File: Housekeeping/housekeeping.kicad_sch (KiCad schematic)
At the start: 2 parts

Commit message: DCDCconverter modified
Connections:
- net 9V renamed 12V
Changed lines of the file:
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@@
 		)
 	)
-	(hierarchical_label "9V"
+	(hierarchical_label "12V"
 		(shape input)
 		(at 133.35 80.01 180)
@@
 			(project "Supercap"
 				(path "/98ee8313-37ab-4329-91ab-b5710476f82f/47f13d7b-df0e-4361-81b8-c133778882c5"
-					(reference "P7809B-1000R")
-					(unit 1)
-				)
+					(reference "P7812B-1000R")
+					(unit 1)
+				)

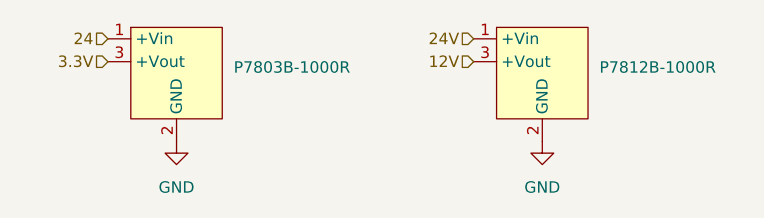
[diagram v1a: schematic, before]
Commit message: removed v1 files and assigned mouser part numbers
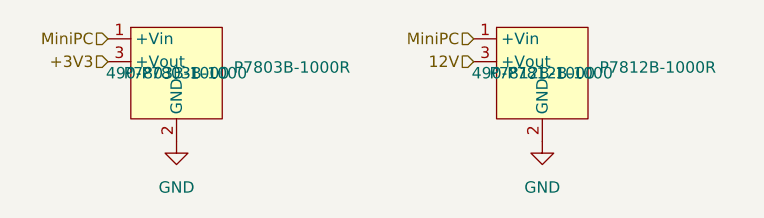
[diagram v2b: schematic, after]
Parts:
- P7803B-1000R: Manufacturer_Part_Number (none) -> P7803B-1000; Mouser Part Number (none) -> 490-P7803B-1000
- P7812B-1000R: Manufacturer_Part_Number (none) -> P7812B-1000; Mouser Part Number (none) -> 490-P7812B-1000
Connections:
- net 24V is gone; now on net MiniPC: P7812B-1000R.1 (+Vin)
- net 24 renamed MiniPC
- net 3.3V renamed +3V3
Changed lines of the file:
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@@
 	(generator_version "9.0")
 	(paper "A4")
-	(hierarchical_label "24"
+	(hierarchical_label "MiniPC"
 		(shape input)
 		(at 92.71 77.47 180)
@@
 		)
 	)
-	(hierarchical_label "3.3V"
+	(hierarchical_label "+3V3"
 		(shape input)
 		(at 92.71 80.01 180)
@@
 		)
 	)
-	(hierarchical_label "24V"
+	(hierarchical_label "MiniPC"
 		(shape input)
 		(at 133.35 77.47 180)
@@
 			)
 		)
+		(property "Manufacturer_Part_Number" "P7812B-1000"
+			(at 140.97 81.28 0)
+			(effects
+				(font
+					(size 1.27 1.27)
+				)
+			)
+		)
+		(property "Mouser Part Number" "490-P7812B-1000"
+			(at 140.97 81.28 0)
+			(effects
+				(font
+					(size 1.27 1.27)
+				)
+			)
+		)
 		(pin "1"
 		)
@@
 			)
 		)
+		(property "Manufacturer_Part_Number" "P7803B-1000"
+			(at 100.33 81.28 0)
+			(effects
+				(font
+					(size 1.27 1.27)
+				)
+			)
+		)
+		(property "Mouser Part Number" "490-P7803B-1000"
+			(at 100.33 81.28 0)
+			(effects
+				(font
+					(size 1.27 1.27)
+				)
+			)
+		)

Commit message: began layout
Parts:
- P7803B-1000R1: renamed from P7803B-1000R; value ~ -> P7803B-1000; footprint P78B-1000R series:P78B-1000R -> Robomaster_ICs:P7812B1000; symbol P78B-1000R series:P78B-1000R -> Robomaster_IV:P7803B-1000; Height (none) -> 10.45; Manufacturer_Name (none) -> CUI Inc.; Mouser Price/Stock (none) -> https://www.mouser.com/ProductDetail/CUI-Inc/P7803B-1000?qs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
- P7812B-1000R1: renamed from P7812B-1000R; value ~ -> 490-P7812B-1000; footprint P78B-1000R series:P78B-1000R -> Robomaster_ICs:P7812B1000; symbol P78B-1000R series:P78B-1000R -> Robomaster_IV:P7812B-1000; Height (none) -> 10.45; Manufacturer_Name (none) -> CUI Inc.; Mouser Price/Stock (none) -> https://www.mouser.com/ProductDetail/CUI-Inc/P7812B-1000?qs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
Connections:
- net 12V renamed +12V
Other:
- note added: "3V3 DC/DC"
- note added: "Gate Driver V_{cc} DC/DC"
- moved on the sheet: P7803B-1000R1, P7812B-1000R1

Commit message: mostly done with first order layout
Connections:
- net MiniPC: no longer P7812B-1000R1.1 (+VIN)
- new net +24V: P7812B-1000R1.1 (+VIN)
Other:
- company: (none) -> UT Robomaster
- title: (none) -> Housekeeping Board
- moved on the sheet: P7803B-1000R1, P7812B-1000R1
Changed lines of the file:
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@@
 	(generator_version "9.0")
 	(paper "A4")
+	(title_block
+		(title "Housekeeping Board")
+		(date "10/18/2025")
+		(rev "1")
+		(company "UT Robomaster")
+		(comment 1 "Robomaster")
+	)
 	(rectangle
-		(start 80.01 78.74)
-		(end 138.43 99.06)
+		(start 118.11 93.98)
+		(end 176.53 114.3)
 		(stroke
 			(width 0.635)
@@
 	)
 	(rectangle
-		(start 80.01 54.61)
-		(end 138.43 74.93)
+		(start 118.11 69.85)
+		(end 176.53 90.17)
 		(stroke
 			(width 0.635)
@@
 	(text "Gate Driver V_{cc} DC/DC"
 		(exclude_from_sim no)
-		(at 136.906 96.52 0)
+		(at 175.006 111.76 0)
 		(effects
 			(font
@@
 	(text "3V3 DC/DC"
 		(exclude_from_sim no)
-		(at 137.16 72.644 0)
+		(at 175.26 87.884 0)
 		(effects
 			(font
@@
 	(wire
 		(pts
-			(xy 92.71 91.44) (xy 92.71 86.36)
-		)
-		(stroke
-			(width 0)
-			(type default)
-		)
-	)
-	(wire
-		(pts
-			(xy 91.44 64.77) (xy 97.79 64.77)
-		)
-		(stroke
-			(width 0)
-			(type default)
-		)
-	)
-	(wire
-		(pts
-			(xy 93.98 62.23) (xy 93.98 67.31)
-		)
-		(stroke
-			(width 0)
-			(type default)
-		)
-	)
-	(wire
-		(pts
-			(xy 97.79 62.23) (xy 93.98 62.23)
-		)
-		(stroke
-			(width 0)
-			(type default)
-		)
-	)
-	(wire
-		(pts
-			(xy 90.17 88.9) (xy 96.52 88.9)
-		)
-		(stroke
-			(width 0)
-			(type default)
-		)
-	)
-	(wire
-		(pts
-			(xy 91.44 59.69) (xy 97.79 59.69)
-		)
-		(stroke
-			(width 0)
-			(type default)
-		)
-	)
-	(wire
-		(pts
-			(xy 92.71 86.36) (xy 96.52 86.36)
-		)
-		(stroke
-			(width 0)
-			(type default)
-		)
-	)
-	(wire
-		(pts
-			(xy 90.17 83.82) (xy 96.52 83.82)
+			(xy 130.81 106.68) (xy 130.81 101.6)
+		)
+		(stroke
+			(width 0)
+			(type default)
+		)
+	)
+	(wire
+		(pts
+			(xy 129.54 80.01) (xy 135.89 80.01)
+		)
+		(stroke
+			(width 0)
+			(type default)
+		)
+	)
+	(wire
+		(pts
+			(xy 132.08 77.47) (xy 132.08 82.55)
+		)
+		(stroke
+			(width 0)
+			(type default)
+		)
+	)
+	(wire
+		(pts
+			(xy 135.89 77.47) (xy 132.08 77.47)
+		)
+		(stroke
+			(width 0)
+			(type default)
+		)
+	)
+	(wire
+		(pts
+			(xy 128.27 104.14) (xy 134.62 104.14)
+		)
+		(stroke
+			(width 0)
+			(type default)
+		)
+	)
+	(wire
+		(pts
+			(xy 129.54 74.93) (xy 135.89 74.93)
+		)
+		(stroke
+			(width 0)
+			(type default)
+		)
+	)
+	(wire
+		(pts
+			(xy 130.81 101.6) (xy 134.62 101.6)
+		)
+		(stroke
+			(width 0)
+			(type default)
+		)
+	)
+	(wire
+		(pts
+			(xy 128.27 99.06) (xy 134.62 99.06)
 		)
 		(stroke
@@
 	(hierarchical_label "MiniPC"
 		(shape input)
-		(at 91.44 59.69 180)
+		(at 129.54 74.93 180)
 		(effects
 			(font
@@
 	(hierarchical_label "+3V3"
 		(shape input)
-		(at 91.44 64.77 180)
+		(at 129.54 80.01 180)
 		(effects
 			(font
@@
 		)
 	)
-	(hierarchical_label "MiniPC"
+	(hierarchical_label "+24V"
 		(shape input)
-		(at 90.17 83.82 180)
+		(at 128.27 99.06 180)
 		(effects
 			(font
@@
 	(hierarchical_label "+12V"
 		(shape input)
-		(at 90.17 88.9 180)
+		(at 128.27 104.14 180)
 		(effects
 			(font
@@
 	(symbol
 		(lib_id "power:GND")
-		(at 92.71 91.44 0)
+		(at 130.81 106.68 0)
 		(unit 1)
 		(exclude_from_sim no)
@@
 		(dnp no)
 		(fields_autoplaced yes)
-		(property "Reference" "#PWR015"
-			(at 92.71 97.79 0)
+		(property "Reference" "#PWR019"
+			(at 130.81 113.03 0)
 			(effects
 				(font
@@
 		)
 		(property "Value" "GND"
-			(at 92.71 96.52 0)
+			(at 130.81 111.76 0)
 			(effects
 				(font
@@
 		)
 		(property "Footprint" ""
-			(at 92.71 91.44 0)
+			(at 130.81 106.68 0)
 			(effects
 				(font
@@
 		)
 		(property "Datasheet" ""
-			(at 92.71 91.44 0)
+			(at 130.81 106.68 0)
 			(effects
 				(font
@@
 		)
 		(property "Description" "Power symbol creates a global label with name \"GND\" , ground"
-			(at 92.71 91.44 0)
+			(at 130.81 106.68 0)
 			(effects
 				(font
@@
 			(project ""
 				(path "/98ee8313-37ab-4329-91ab-b5710476f82f/47f13d7b-df0e-4361-81b8-c133778882c5"
-					(reference "#PWR015")
+					(reference "#PWR019")
 					(unit 1)
 				)
@@
 	(symbol
 		(lib_id "power:GND")
-		(at 93.98 67.31 0)
+		(at 132.08 82.55 0)
 		(unit 1)
 		(exclude_from_sim no)
@@
 		(dnp no)
 		(fields_autoplaced yes)
-		(property "Reference" "#PWR016"
-			(at 93.98 73.66 0)
+		(property "Reference" "#PWR020"
+			(at 132.08 88.9 0)
 			(effects
 				(font
@@
 		)
 		(property "Value" "GND"
-			(at 93.98 72.39 0)
+			(at 132.08 87.63 0)
 			(effects
 				(font
@@
 		)
 		(property "Footprint" ""
-			(at 93.98 67.31 0)
+			(at 132.08 82.55 0)
 			(effects
 				(font
@@
 		)
 		(property "Datasheet" ""
-			(at 93.98 67.31 0)
+			(at 132.08 82.55 0)
 			(effects
 				(font
@@
 		)
 		(property "Description" "Power symbol creates a global label with name \"GND\" , ground"
-			(at 93.98 67.31 0)
+			(at 132.08 82.55 0)
 			(effects
 				(font
@@
 			(project "Supercap"
 				(path "/98ee8313-37ab-4329-91ab-b5710476f82f/47f13d7b-df0e-4361-81b8-c133778882c5"
-					(reference "#PWR016")
+					(reference "#PWR020")
 					(unit 1)
 				)
@@
 		(lib_name "P7812B-1000_1")
 		(lib_id "Robomaster_IV:P7812B-1000")
-		(at 96.52 83.82 0)
+		(at 134.62 99.06 0)
 		(unit 1)
 		(exclude_from_sim no)
@@
 		(fields_autoplaced yes)
 		(property "Reference" "P7812B-1000R1"
-			(at 118.11 85.0899 0)
+			(at 156.21 100.3299 0)
 			(effects
 				(font
@@
 		)
 		(property "Value" "490-P7812B-1000"
-			(at 118.11 87.6299 0)
+			(at 156.21 102.8699 0)
 			(effects
 				(font
@@
 		)
 		(property "Footprint" "Robomaster_ICs:P7812B1000"
-			(at 118.11 178.74 0)
+			(at 156.21 193.98 0)
 			(effects
 				(font
@@
 		)
 		(property "Datasheet" "https://www.cui.com/product/resource/p78b-1000.pdf"
-			(at 118.11 278.74 0)
+			(at 156.21 293.98 0)
 			(effects
 				(font
@@
 		)
 		(property "Description" "Non-Isolated DC/DC Converters dc-dc non-isolated, 1.0 A, 15-32 Vdc input, 12 Vdc output, SIP"
-			(at 96.52 83.82 0)
+			(at 134.62 99.06 0)
 			(effects
 				(font
@@
 		)
 		(property "Manufacturer_Part_Number" "P7812B-1000"
-			(at 118.11 878.74 0)
+			(at 156.21 893.98 0)
 			(effects
 				(font
@@
 		)
 		(property "Mouser Part Number" "490-P7812B-1000"
-			(at 118.11 578.74 0)
+			(at 156.21 593.98 0)
 			(effects
 				(font
@@
 		)
 		(property "Height" "10.45"
-			(at 118.11 478.74 0)
+			(at 156.21 493.98 0)
 			(effects
 				(font
@@
 		)
 		(property "Mouser Price/Stock" "https://www.mouser.com/ProductDetail/CUI-Inc/P7812B-1000?qs=IKkN%2F947nfBpDKODYyx3RQ%3D%3D"
-			(at 118.11 678.74 0)
+			(at 156.21 693.98 0)
 			(effects
 				(font
@@
 		)
 		(property "Manufacturer_Name" "CUI Inc."
-			(at 118.11 778.74 0)
+			(at 156.21 793.98 0)
 			(effects
 				(font
@@
 	(symbol
 		(lib_id "Robomaster_IV:P7803B-1000")
-		(at 97.79 59.69 0)
+		(at 135.89 74.93 0)
 		(unit 1)
 		(exclude_from_sim no)
@@
 		(fields_autoplaced yes)
 		(property "Reference" "P7803B-1000R1"
-			(at 119.38 60.9599 0)
+			(at 157.48 76.1999 0)
 			(effects
 				(font
@@
 		)
 		(property "Value" "P7803B-1000"
-			(at 119.38 63.4999 0)
+			(at 157.48 78.7399 0)
 			(effects
 				(font
@@
 		)
 		(property "Footprint" "Robomaster_ICs:P7812B1000"
-			(at 119.38 154.61 0)
+			(at 157.48 169.85 0)
 			(effects
 				(font
@@
 		)
 		(property "Datasheet" "https://www.cui.com/product/resource/p78b-1000.pdf"
-			(at 119.38 254.61 0)
+			(at 157.48 269.85 0)
 			(effects
 				(font
@@
 		)
 		(property "Description" "Non-Isolated DC/DC Converters dc-dc non-isolated, 1.0 A, 15-32 Vdc input, 12 Vdc output, SIP"
-			(at 97.79 59.69 0)
+			(at 135.89 74.93 0)
 			(effects
 				(font
@@
 		)
 		(property "Manufacturer_Part_Number" "P7803B-1000"
-			(at 119.38 854.61 0)
+			(at 157.48 869.85 0)
 			(effects
 				(font
@@
 		)
 		(property "Mouser Part Number" "490-P7803B-1000"
-			(at 119.38 554.61 0)
+			(at 157.48 569.85 0)
 			(effects
 				(font
@@
 		)
 		(property "Height" "10.45"
-			(at 119.38 454.61 0)
+			(at 157.48 469.85 0)
 			(effects
 				(font
@@
 		)
 		(property "Mouser Price/Stock" "https://www.mouser.com/ProductDetail/CUI-Inc/P7803B-1000?qs=IKkN%2F947nfBpDKODYyx3RQ%3D%3D"
-			(at 119.38 654.61 0)
+			(at 157.48 669.85 0)
 			(effects
 				(font
@@
 		)
 		(property "Manufacturer_Name" "CUI Inc."
-			(at 119.38 754.61 0)
-			(effects
-				(font
+			(at 157.48 769.85 0)
+			(effects
+				(font

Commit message: big progress on layout
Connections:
- net GND: no longer P7812B-1000R1.2 (GND)
- new net GNDPWR: P7812B-1000R1.2 (GND)
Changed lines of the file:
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@@
 	)
 	(symbol
-		(lib_id "power:GND")
+		(lib_id "power:GNDPWR")
 		(at 130.81 106.68 0)
 		(unit 1)
@@
 		(dnp no)
 		(fields_autoplaced yes)
-		(property "Reference" "#PWR019"
-			(at 130.81 113.03 0)
+		(property "Reference" "#PWR032"
+			(at 130.81 111.76 0)
 			(effects
 				(font
@@
 			)
 		)
-		(property "Value" "GND"
-			(at 130.81 111.76 0)
+		(property "Value" "GNDPWR"
+			(at 130.683 110.49 0)
 			(effects
 				(font
@@
 		)
 		(property "Footprint" ""
-			(at 130.81 106.68 0)
+			(at 130.81 107.95 0)
 			(effects
 				(font
@@
 		)
 		(property "Datasheet" ""
-			(at 130.81 106.68 0)
+			(at 130.81 107.95 0)
 			(effects
 				(font
@@
 			)
 		)
-		(property "Description" "Power symbol creates a global label with name \"GND\" , ground"
+		(property "Description" "Power symbol creates a global label with name \"GNDPWR\" , global ground"
 			(at 130.81 106.68 0)
 			(effects
@@
 		)
 		(instances
-			(project "housekeeping"
-				(path "/54dd3bdb-fa85-45ef-ba5f-b0f6c4bf9e9e"
-					(reference "#PWR?")
+			(project "Supercap"
+				(path "/98ee8313-37ab-4329-91ab-b5710476f82f/47f13d7b-df0e-4361-81b8-c133778882c5"
+					(reference "#PWR032")
 					(unit 1)
 				)
-			)
-			(project ""
-				(path "/98ee8313-37ab-4329-91ab-b5710476f82f/47f13d7b-df0e-4361-81b8-c133778882c5"
-					(reference "#PWR019")
-					(unit 1)
-				)

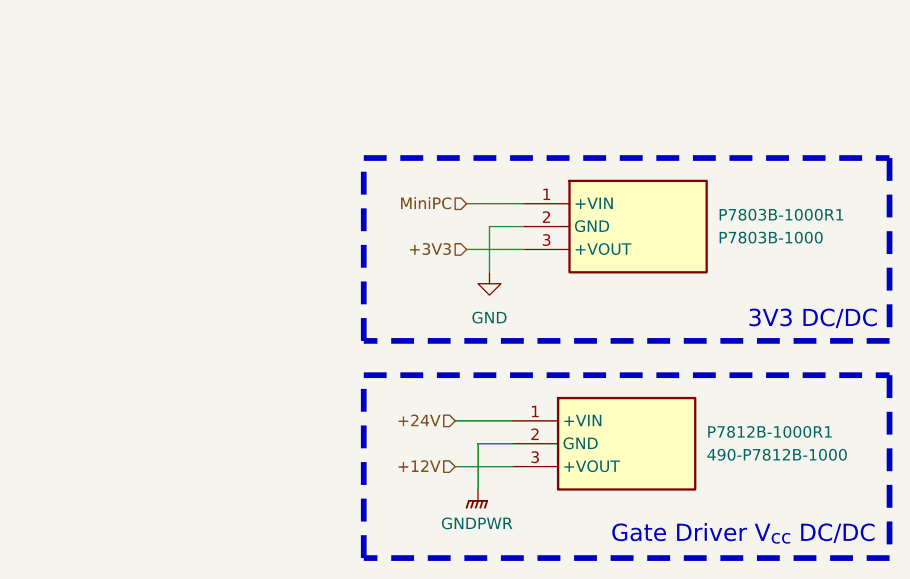
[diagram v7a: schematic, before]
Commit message: added better smoothing behavior to power supplies and op-amps as per application notes, switched resistors to op-amp with higher values
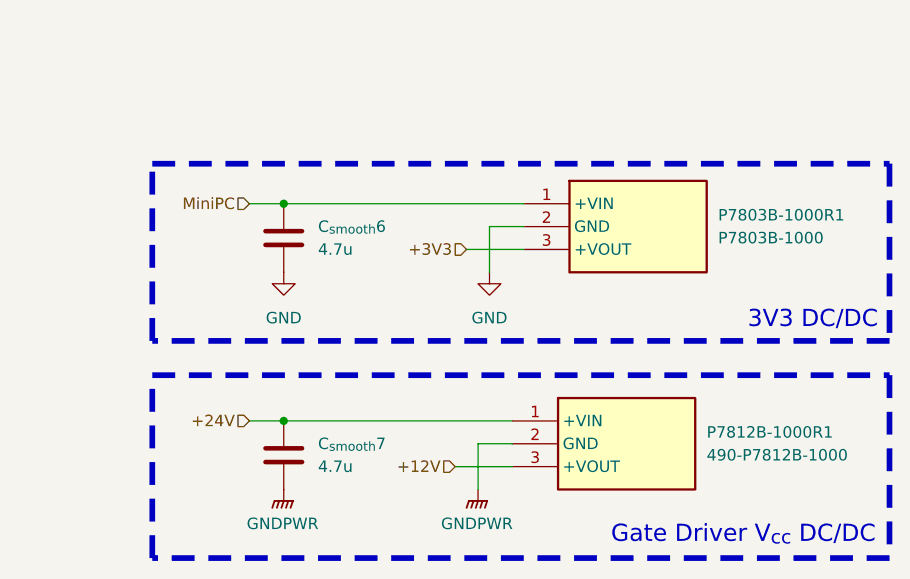
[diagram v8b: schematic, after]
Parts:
- added C_{smooth}6, C_{smooth}7: 4.7u, Capacitor_SMD:C_0603_1608Metric_Pad1.08x0.95mm_HandSolder, symbol Device:C
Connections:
- net +24V: now also C_{smooth}7.1
- net GND: now also C_{smooth}6.2
- net GNDPWR: now also C_{smooth}7.2
- net MiniPC: now also C_{smooth}6.1
